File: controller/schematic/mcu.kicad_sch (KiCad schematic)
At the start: 32 parts, among them J2 TYPE-C-31-M-12, J4 1WIRE, J5 1WIRE, J6 1WIRE, J7 1WIRE, U1 ESP32-C6-WROOM-1-N8, U4 USBLC6-2SC6, U5 TMP1075D

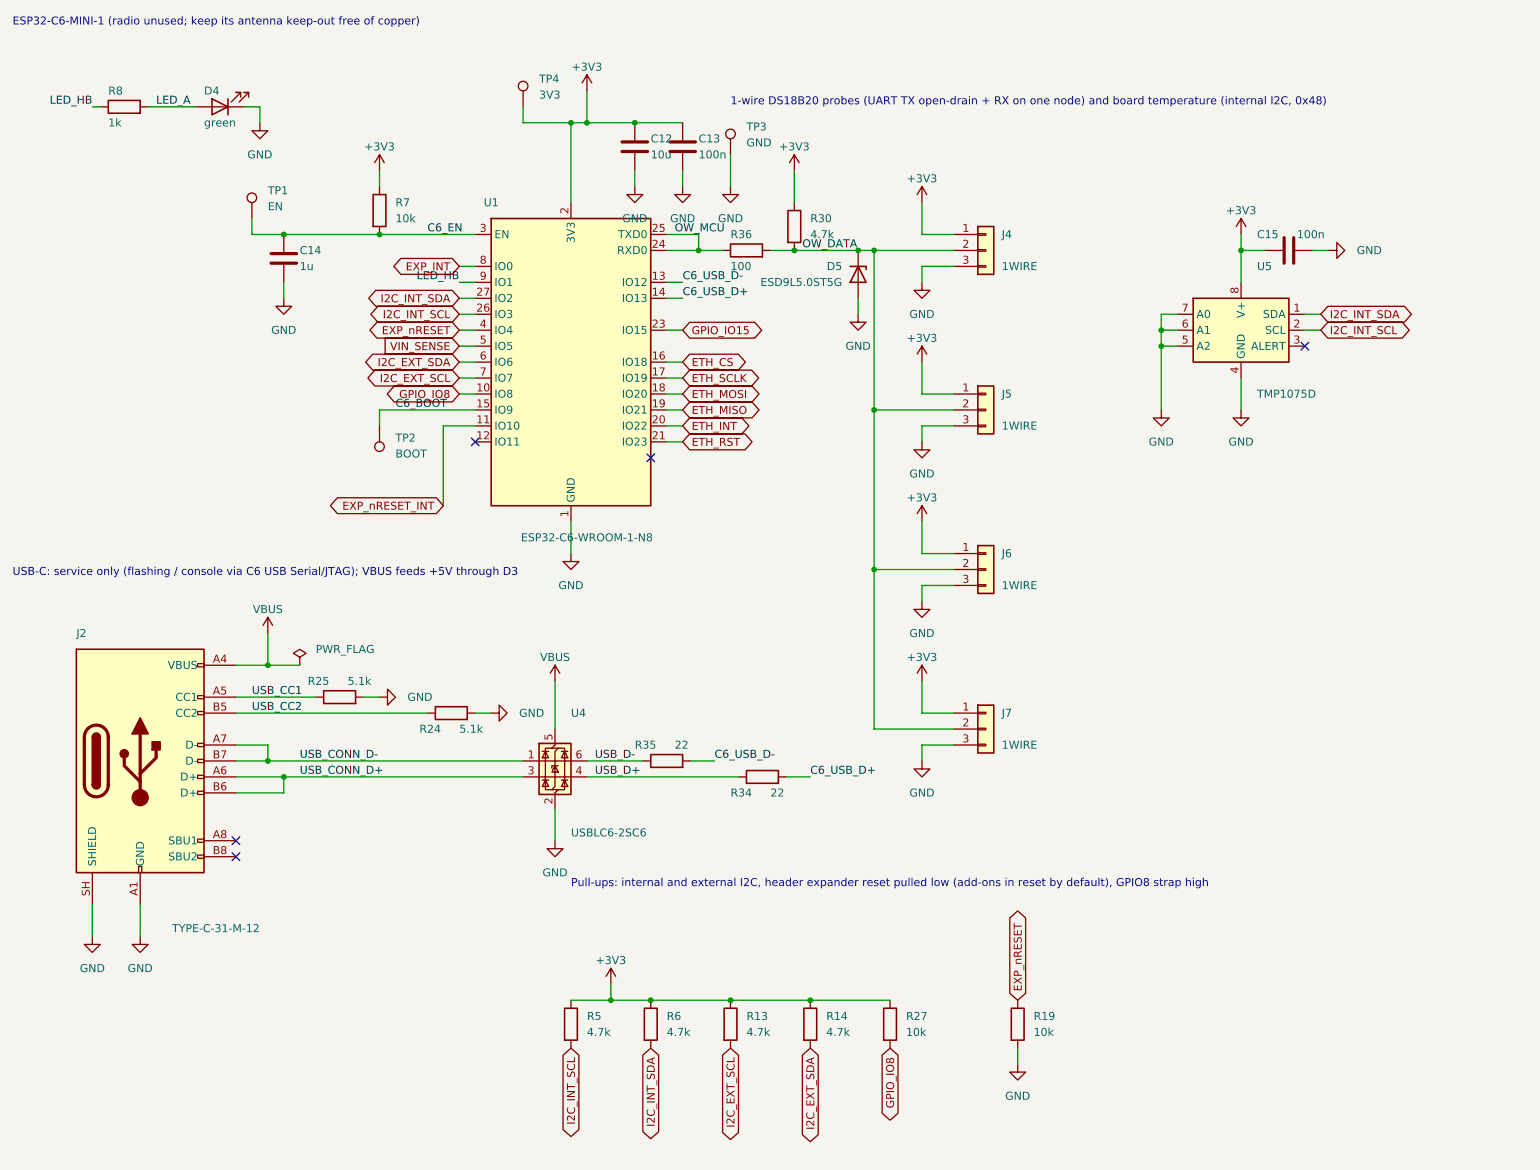
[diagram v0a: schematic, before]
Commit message: controller: rev D schematic - node section (relays sheet: J11-J18, K1-K16, U14-U17 and passives), J8 expansion header network (RN2, U7, F2, D7, R19, EXP_nRESET) and the 19 V input (J3, F3, D1, D8) removed; two 12 V PH 2p inputs J11 / J12 OR-ed by SS34 D10 / D11 with SMAJ15A D12 (C148216), VIN_SENSE divider 68k / 10k; new Plane link sheet: J13 / J14 PH 5p, 2.2k SDA / SCL and 10k EXP_INT pull-ups, 33R series, TPD4E05U06 U19 / U20, TPS2553DBVR load switches U21 / U22 (C55266, R_ILIM 180k, 129-174 mA) with a granite:TPS2553DBV symbol; MCU: plane link on GPIO2/3, TMP1075 and J9 on the local bus GPIO6/7, dry inputs on GPIO10/11/4/15, rev C GPIO4 pull-down gone; title blocks rev D; ERC 0, netlist pin map checked
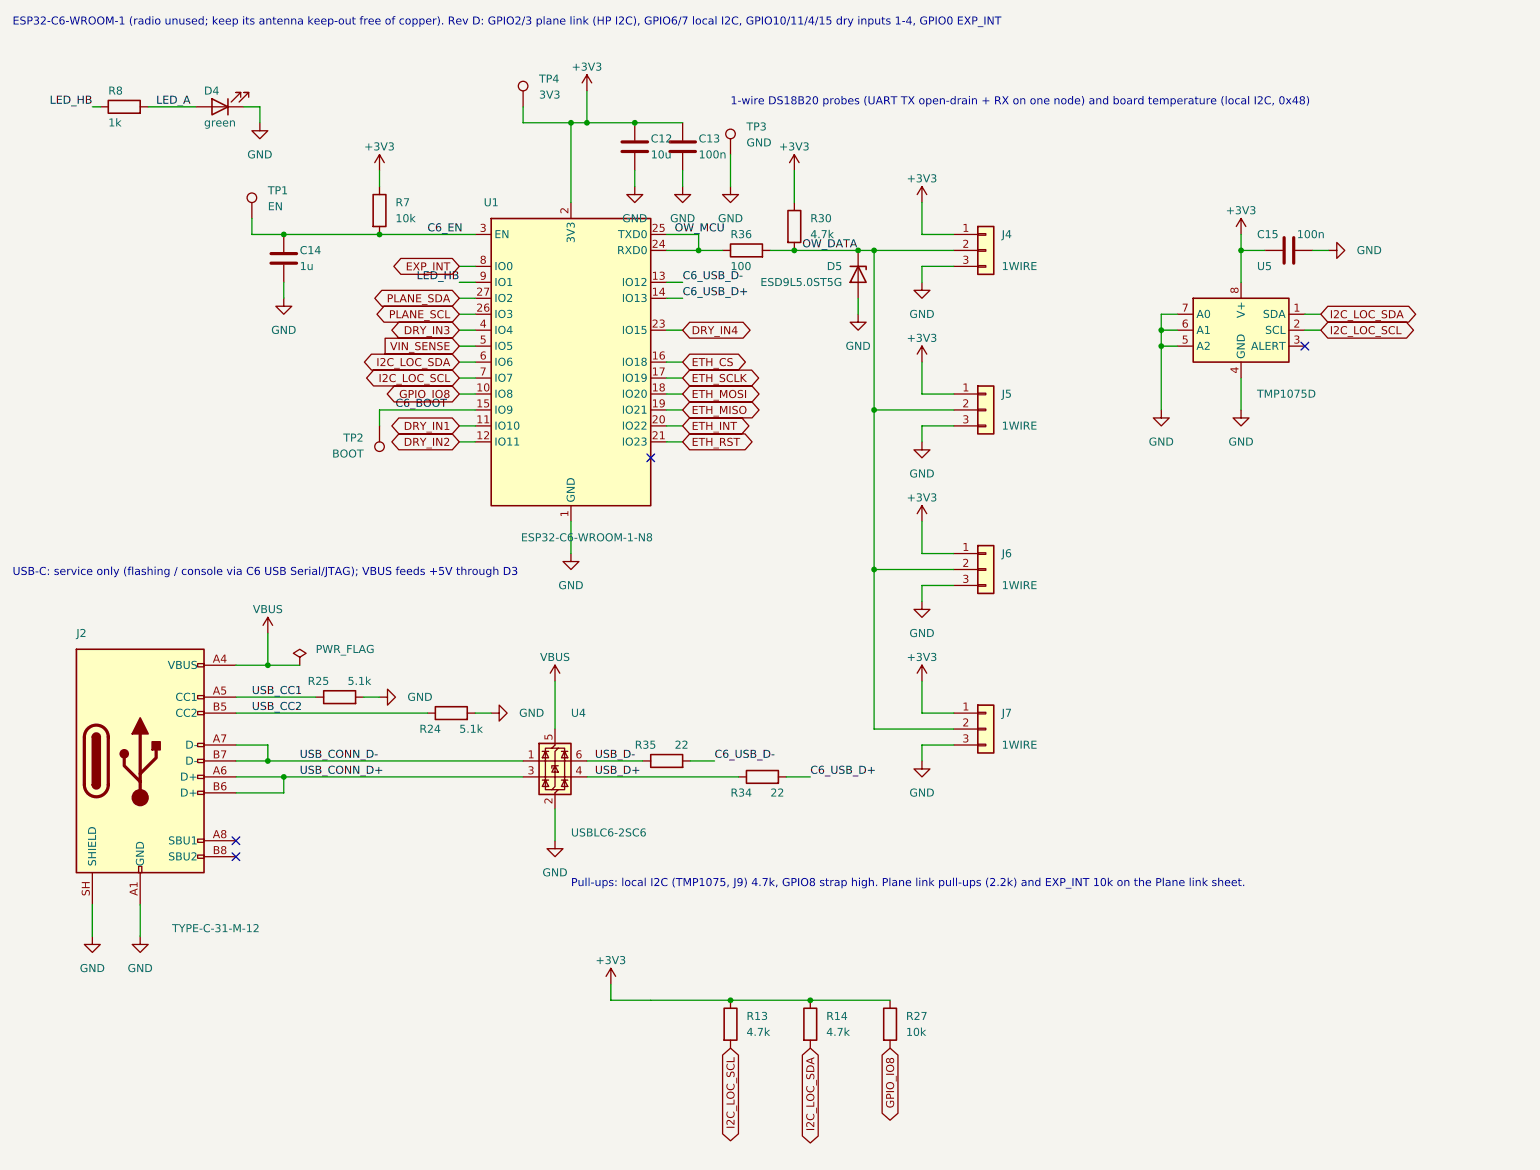
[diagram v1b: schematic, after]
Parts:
- removed R19: 10k, Resistor_SMD:R_0402_1005Metric, symbol Device:R
- removed R5, R6: 4.7k, Resistor_SMD:R_0402_1005Metric, symbol Device:R
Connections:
- net DRY_IN2: now reaches U1.12 (IO11)
- net EXP_nRESET renamed DRY_IN3
- net EXP_nRESET_INT renamed DRY_IN1
- net GPIO_IO15 renamed DRY_IN4
- net I2C_EXT_SCL renamed I2C_LOC_SCL
- net I2C_LOC_SCL: now also U5.2 (SCL)
- net I2C_EXT_SDA renamed I2C_LOC_SDA
- net I2C_LOC_SDA: now also U5.1 (SDA)
- net I2C_INT_SCL renamed PLANE_SCL
- net PLANE_SCL: no longer U5.2 (SCL)
- net I2C_INT_SDA renamed PLANE_SDA
- net PLANE_SDA: no longer U5.1 (SDA)
- no-connect marks 5 -> 4
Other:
- note added: "1-wire DS18B20 probes (UART TX open-drain + RX on one node) and board temperature (local I2C, 0x48)"
- note added: "ESP32-C6-WROOM-1 (radio unused; keep its antenna keep-out free of copper). Rev D: GPIO2/3 plane link (HP I2C), GPIO6/7 local I2C, GPIO10/11/4/15 dry inputs 1-4, GPIO0 EXP_INT"
- note added: "Pull-ups: local I2C (TMP1075, J9) 4.7k, GPIO8 strap high. Plane link pull-ups (2.2k) and EXP_INT 10k on the Plane link sheet."
- note removed: "1-wire DS18B20 probes (UART TX open-drain + RX on one node) and board temperature (internal I2C, 0x48)"
- note removed: "ESP32-C6-MINI-1 (radio unused; keep its antenna keep-out free of copper)"
- note removed: "Pull-ups: internal and external I2C, header expander reset pulled low (add-ons in reset by default), GPIO8 strap high"
- title: Granite Controller - MCU -> Granite controller rev D - MCU
